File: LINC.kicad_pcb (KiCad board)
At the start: 4 copper layers, 55.1 x 58 mm, 44 parts, among them J1 112-024-113R001, J2 FTSH-105-01-L-DV-K, J3 RJHSE5380, J4 USB4085-GF-A, U1 SN74LVC8T245PWR, U2 SN74LVC07APWR, U3 STM32H533RETx, U4 PTS645SH43SMTR92 LFS, U5 THVD1451D, U6 SN74LVC1G07DCKR, U7 SN74LVC14APWR, U8 USBLC6-2SC6, U9 TPSM861253RDXR, Y1 MU00525-32.768K, Y2 CS10820-24M

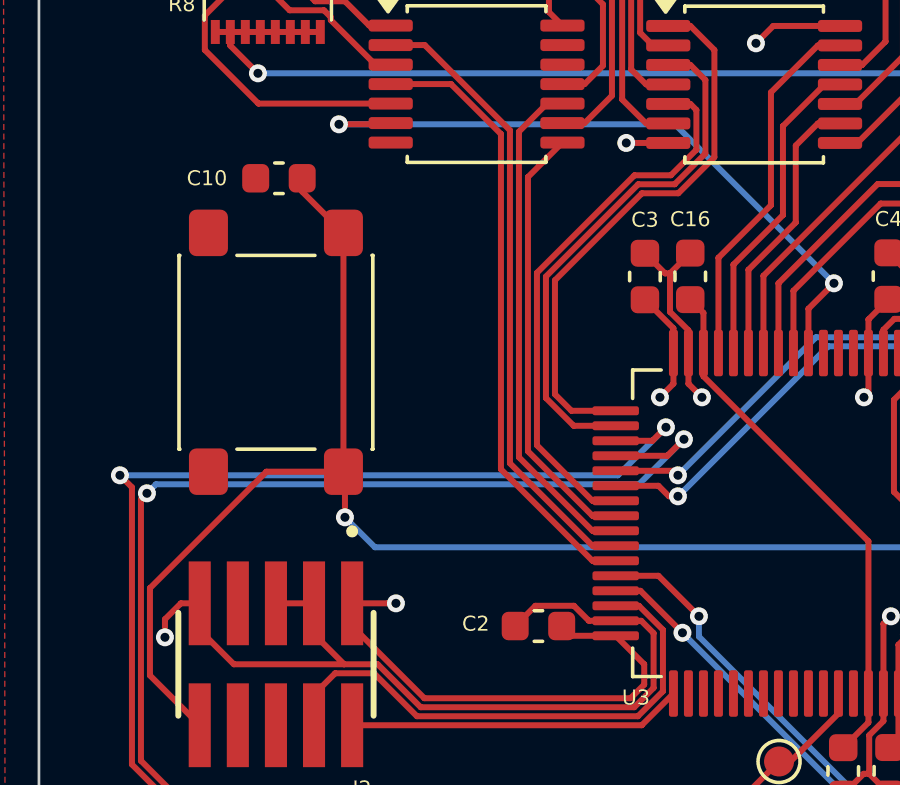
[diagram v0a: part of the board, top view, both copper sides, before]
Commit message: Update graphics and license
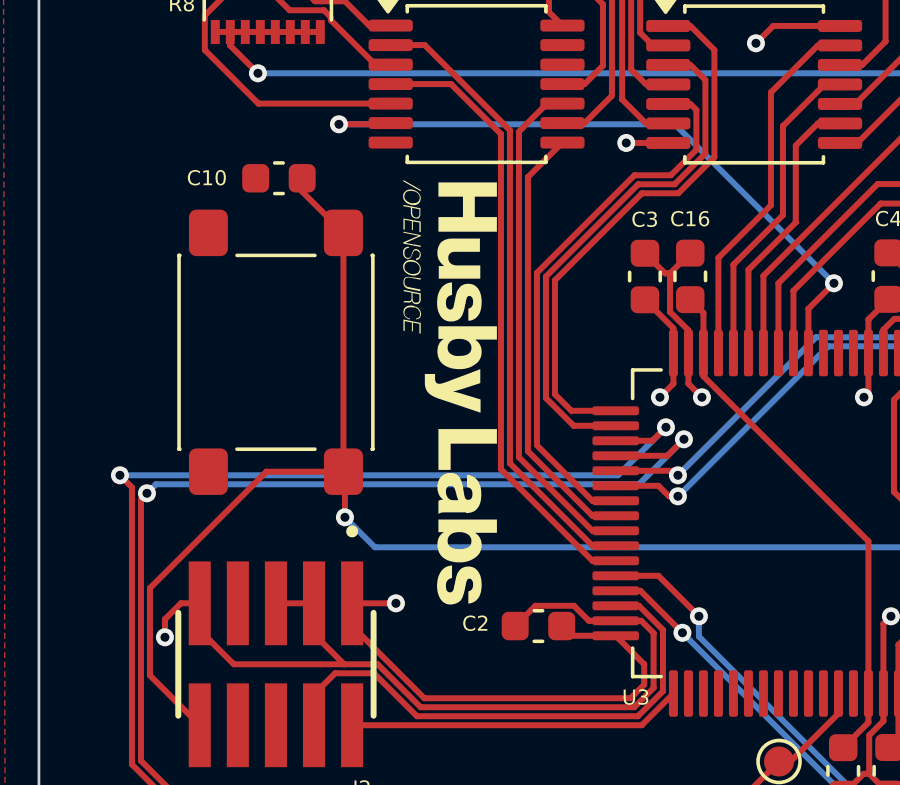
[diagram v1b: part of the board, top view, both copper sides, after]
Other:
- board text added: "Designed in Chicago"
- board text added: "GPIB"
- board text added: "© 2026 Husby Labs Licenced under CERN-OHL-P v2"

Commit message: Ready for release
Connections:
- U3 pad 1: unconnected-(U3A-VBAT-Pad1) -> +3V3
- U3 pad 12: unconnected-(U3A-VSSA-Pad12) -> GND
- U3 pad 13: unconnected-(U3A-VDDA-Pad13) -> +3V3
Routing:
- net GND: track 130.6 -> 136.3 mm
- net +3V3: track 53.0 -> 56.5 mm, vias 9 -> 10
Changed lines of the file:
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@@
 			(layers "F.Cu" "F.Mask" "F.Paste")
 			(roundrect_rratio 0.25)
-			(net "unconnected-(U3A-VBAT-Pad1)")
+			(net "+3V3")
 			(pinfunction "VBAT_1")
-			(pintype "power_in+no_connect")
+			(pintype "power_in")
 		)
 		(pad "2" smd roundrect
@@
 			(layers "F.Cu" "F.Mask" "F.Paste")
 			(roundrect_rratio 0.25)
-			(net "unconnected-(U3A-VSSA-Pad12)")
+			(net "GND")
 			(pinfunction "VSSA_12")
-			(pintype "power_in+no_connect")
+			(pintype "power_in")
 		)
 		(pad "13" smd roundrect
@@
 			(layers "F.Cu" "F.Mask" "F.Paste")
 			(roundrect_rratio 0.25)
-			(net "unconnected-(U3A-VDDA-Pad13)")
+			(net "+3V3")
 			(pinfunction "VDDA_13")
-			(pintype "power_in+no_connect")
+			(pintype "power_in")
 		)
 		(pad "14" smd roundrect
@@
 	)
 	(segment
+		(start 170.415501 94.941398)
+		(end 171.990501 94.941398)
+		(width 0.2)
+		(layer "F.Cu")
+		(net "GND")
+	)
+	(segment
 		(start 168.660501 119.046398)
 		(end 169.960501 119.046398)
@@
 	)
 	(segment
+		(start 169.440501 95.916398)
+		(end 170.415501 94.941398)
+		(width 0.2)
+		(layer "F.Cu")
+		(net "GND")
+	)
+	(segment
 		(start 153.640501 100.416398)
 		(end 152.965501 101.091398)
@@
 	)
 	(segment
+		(start 167.665501 95.916398)
+		(end 169.440501 95.916398)
+		(width 0.2)
+		(layer "F.Cu")
+		(net "GND")
+	)
+	(segment
 		(start 163.900501 106.756398)
 		(end 163.900501 106.696398)
@@
 	)
 	(segment
+		(start 171.990501 94.941398)
+		(end 172.665501 95.616398)
+		(width 0.2)
+		(layer "F.Cu")
+		(net "GND")
+	)
+	(segment
 		(start 157.578737 103.154634)
 		(end 156.934973 103.798398)
@@
 	)
 	(segment
+		(start 167.615501 101.366398)
+		(end 167.665501 101.416398)
+		(width 0.2)
+		(layer "F.Cu")
+		(net "+3V3")
+	)
+	(segment
 		(start 157.266605 103.042502)
 		(end 156.810709 103.498398)
@@
 	)
 	(segment
+		(start 167.665501 95.416398)
+		(end 168.840501 95.416398)
+		(width 0.2)
+		(layer "F.Cu")
+		(net "+3V3")
+	)
+	(segment
 		(start 158.240501 91.991398)
 		(end 158.240501 91.166398)
@@
 	)
 	(segment
+		(start 166.090501 101.366398)
+		(end 167.615501 101.366398)
+		(width 0.2)
+		(layer "F.Cu")
+		(net "+3V3")
+	)
+	(segment
 		(start 168.143001 81.888898)
 		(end 169.805868 81.888898)
@@
 	)
 	(segment
+		(start 168.840501 95.416398)
+		(end 169.290501 94.966398)
+		(width 0.2)
+		(layer "F.Cu")
+		(net "+3V3")
+	)
+	(segment
 		(start 164.740501 90.871398)
 		(end 164.740501 91.991398)
@@
 		(size 0.6)
 		(drill 0.3)
+		(layers "F.Cu" "B.Cu")
+		(net "+3V3")
+	)
+	(via
+		(at 169.290501 94.966398)
+		(size 0.6)
+		(drill 0.3)
